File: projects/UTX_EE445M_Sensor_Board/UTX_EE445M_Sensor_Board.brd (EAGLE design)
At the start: 44.5 x 20.9 mm, 26 parts, among them IC1 TM4C123GH6PM, Q1 NX5032GA

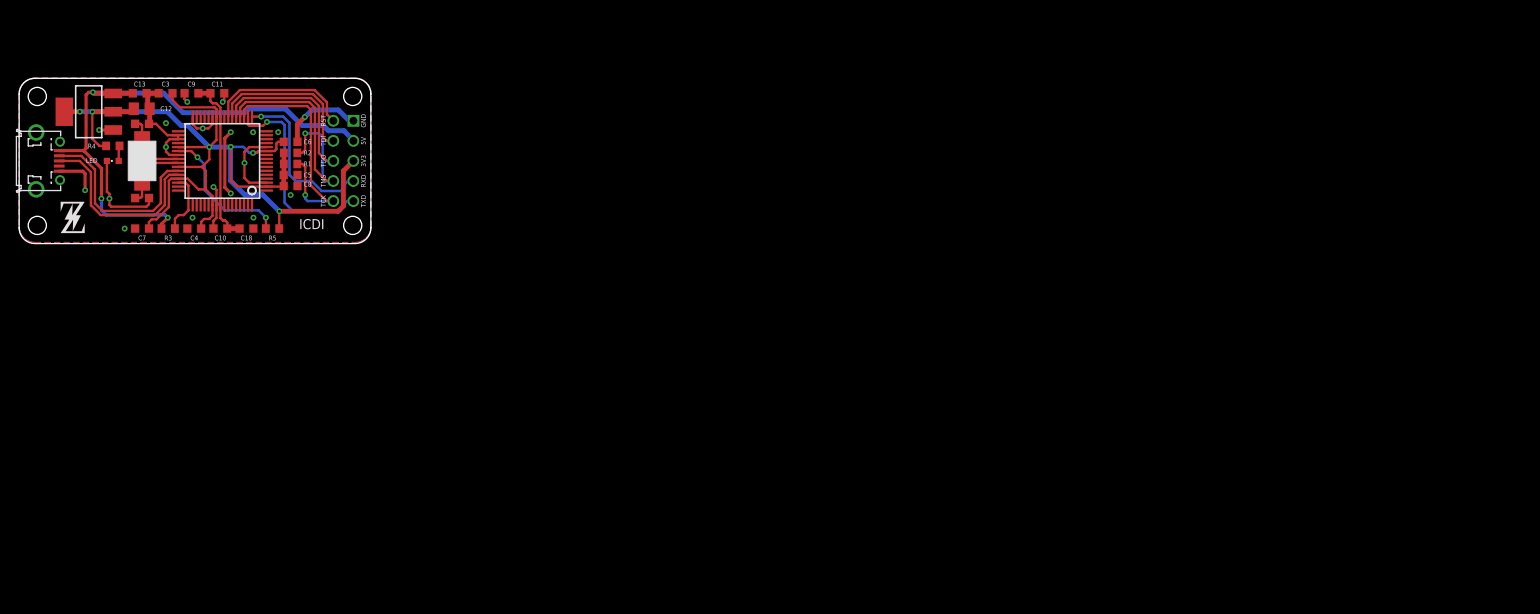
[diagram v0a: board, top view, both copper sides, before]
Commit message: fix some naming and upload UTX EE445M sensor board
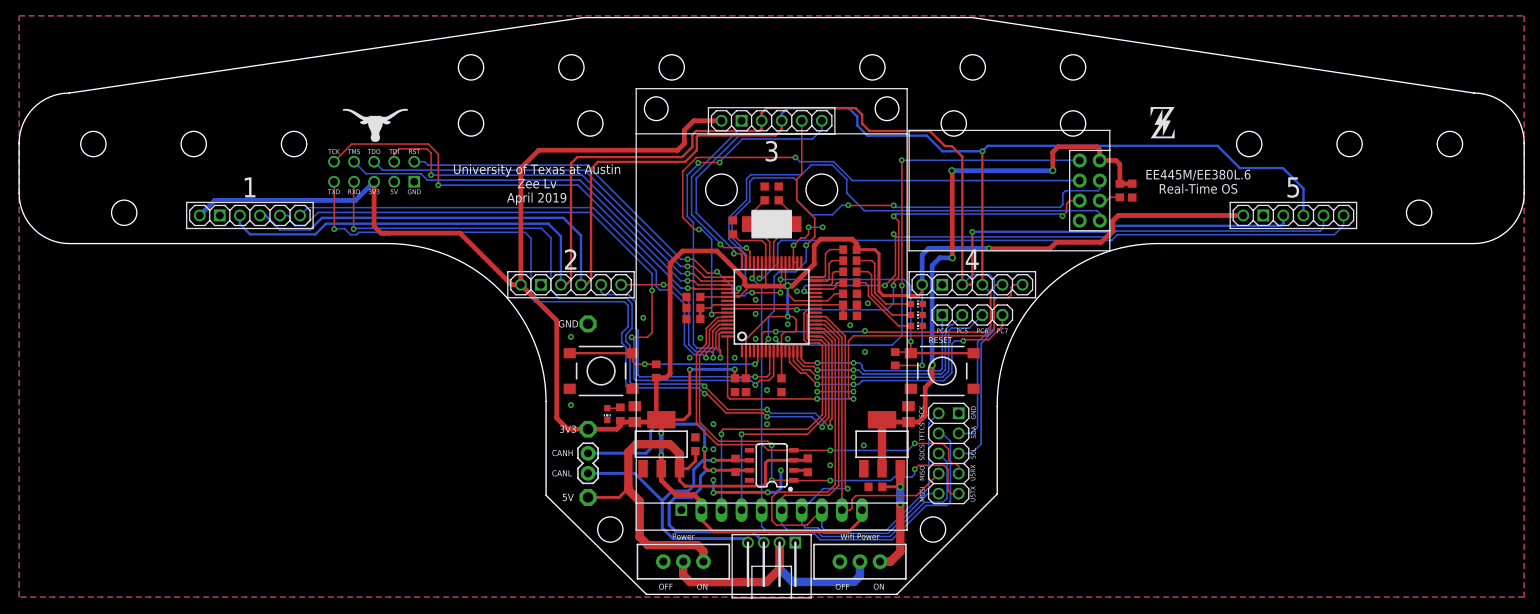
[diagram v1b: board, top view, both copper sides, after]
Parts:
- removed LED: (no value), adafruit:CHIPLED_0603
- added 3V3, 5V, GND: TPPAD1-13, testpad:P1-13
- added BUTTON, RESET: _SWITCH_DTSM-6, Z:_SWITCH_DTSM-6
- added C14: (no value), UT_ECE:C0805K
- added C15: (no value), UT_ECE:C0603K
- added C16, C17: 0.1uF, UT_ECE:C0603K
- added DIS1: ST7735, UT_ECE:ST7735
- added JP1: (no value), UT_ECE:1X02
- added JP2: (no value), UT_ECE:1X04
- added LED1, LED2, LED3, PWR_LED: (no value), led:CHIP-LED0603
- added R6: 120, UT_ECE:R0603
- added R7, R8, R9: 10k, UT_ECE:R0603
- added S1, S2: (no value), SparkFun-Switches:SWITCH_SPDT_PTH_11.6X4.0MM
- added U$10: UTX_EE445M_BOARD_CONNECTOR, Z:_HEADER_2_4X1_ANGLED
- added U$11: LOGIC_ANALYZER_10PIN, Z:LOGIC_ANALYZER_10PIN
- added U$12: (no value), Z:__LOGO_UT_ECE
- added U$13, U$9: _VOLTAGE_REGULATOR_AMS1117, Z:_PACKAGE_SOT223
- added U$14: ESP-01, UT_ECE:ESP8266_01
- added U$5, U$6: LIDAR_VL53L0X_ATK_VERT, Z:LIDAR_VL53L0X_ATK_VERT
- added U$7: (no value), Z:LOGO_LORNHORNS
- added U$8: (no value), Z:LOGO_Z_3X4
- added U4: MCP2551PSOIC, UT_ECE:SO08
- R1, R2, R4: value 10k -> 470
- R3: value 330 -> 470; device UT_ECE:R0603 -> rcl:R0603
- R5: value 10k -> 1M
- U$1: value USB_MICRO_PTH -> JTAG_SERIAL; device Z:USB_MICRO_PTH -> Z:JTAG_SERIAL_PTH
- U$2: value JTAG_SERIAL -> LIDAR_VL53L0X_ATK_VERT; device Z:JTAG_SERIAL_PTH -> Z:LIDAR_VL53L0X_ATK_VERT
- U$3: value (none) -> LIDAR_VL53L0X_ATK_VERT; device Z:__LOGO_Z -> Z:LIDAR_VL53L0X_ATK_VERT
- U$4: value _VOLTAGE_REGULATOR_AMS1117 -> LIDAR_VL53L0X_ATK_VERT; device Z:_PACKAGE_SOT223 -> Z:LIDAR_VL53L0X_ATK_VERT
- moved R4 94.4 mm to (105.2, -2.16)
- moved C3 90.3 mm to (105.2, -6.35), turned to 0 degrees
- moved C9 87.5 mm to (105.2, -7.75), turned to 0 degrees
- moved U$4 86.4 mm to (95.2, 15.5), turned to 0 degrees
- moved C11 84.9 mm to (105.2, -9.14)
- moved C13 83.2 mm to (85.6, -25.4), turned to 90 degrees
- moved C1 81.1 mm to (96.1, 6.35), turned to 90 degrees
- moved Q1 80.1 mm to (95.2, 2.46), turned to 180 degrees
- moved C2 78.8 mm to (94.4, 6.35), turned to 90 degrees
- moved C7 74.8 mm to (90.3, 2.06), turned to 90 degrees
- moved C12 73.4 mm to (77.9, -21.6), turned to 90 degrees
- moved R5 73.1 mm to (105.2, -0.76), turned to 180 degrees
- moved R1 72.4 mm to (105.2, -4.95)
- moved R2 72.4 mm to (105.2, -3.56)
- moved IC1 71.9 mm to (95.2, -8.00), turned to 0 degrees
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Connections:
- net LDO renamed VDDC
- removed net UART0_RX: IC1.17, U$2.RXD
- removed net UART0_TX: IC1.18, U$2.TXD
- removed net USB_DM: IC1.43, U$1.2
- removed net USB_DP: IC1.44, U$1.3
- new net CANH: JP1.2, R6.2, U$10.2, U4.7
- new net CANL: JP1.1, R6.1, U$10.1, U4.6
- new net ESP_3V3: C14.1, C16.1, R9.2, U$13.2, U$13.4, U$14.VCC
- new net ESP_5V: C15.1, S2.1, U$13.3
- new net ESP_GPIO0: IC1.58, U$14.GPIO_0
- new net ESP_GPIO2: IC1.57, U$14.GPIO_2
- new net ESP_RESET: IC1.46, U$14.RESET
- new net I2C0_SCL: IC1.47, U$11.8, U$2.SCL, U$3.SCL, U$4.SCL, U$5.SCL, U$6.SCL
- new net I2C0_SDA: IC1.48, U$11.9, U$2.SDA, U$3.SDA, U$4.SDA, U$5.SDA, U$6.SDA
- new net LOGIC1: IC1.16, JP2.1
- new net LOGIC2: IC1.15, JP2.2
- new net LOGIC3: IC1.14, JP2.3
- new net LOGIC4: IC1.13, JP2.4
- new net N$18: U$1.5V
- new net N$19: IC1.32, R5.2
- new net N$3: S1.3
- new net N$6: PWR_LED.A, R3.1
- new net N$7: LED2.A, R2.1
- new net N$8: LED3.A, R4.1
- new net PF1: IC1.29, R1.2
- new net PF2: IC1.30, R2.2
- new net PF3: IC1.31, R4.2
- new net PF4: BUTTON.1, BUTTON.2, IC1.5, R8.2
- new net RXD: IC1.18, U$1.RXD
- new net SD_CS: DIS1.5, IC1.45, U$11.2
- new net SSI0_MISO: DIS1.9, IC1.21, U$11.4
- new net SSI0_MOSI: DIS1.7, IC1.22, U$11.5
- new net SSI0_SCK: DIS1.8, IC1.19, U$11.1
- new net TFT_CS: DIS1.6, IC1.20, U$11.3
- new net TFT_D/C: DIS1.4, IC1.23
- new net TFT_RESET: DIS1.3, IC1.24
- new net TXD: IC1.17, U$1.TXD
- new net UART2_RX: IC1.53, U$14.TX
- new net UART2_TX: IC1.10, U$14.RX
- new net UART5_RX: IC1.59, U$11.7, U4.4
- new net UART5_TX: IC1.60, U$11.6, U4.1
- new net VIN: S1.2, S2.2, U$10.3
- new net VX_INT1: IC1.9, U$2.INT
- new net VX_INT2: IC1.8, U$3.INT
- new net VX_INT3: IC1.7, U$4.INT
- new net VX_INT4: IC1.6, U$5.INT
- new net VX_INT5: IC1.28, U$6.INT
- new net XSHUT1: IC1.61, U$2.XSH
- new net XSHUT2: IC1.62, U$3.XSH
- new net XSHUT3: IC1.63, U$4.XSH
- new net XSHUT4: IC1.64, U$5.XSH
- new net XSHUT5: IC1.43, U$6.XSH
- net 3V3: now also 3V3.TP, DIS1.10, DIS1.2, R3.2, R5.1, R7.1, R8.1, U$1.3V3, U$2.VCC, U$3.VCC, U$4.VCC, U$5.VCC, U$6.VCC, U$9.2, U$9.4; no longer IC1.45, R1.2, R2.2, R4.2, R5.2, U$2.3V3, U$4.2, U$4.4
- net 5V: now also 5V.TP, C17.1, S1.1, U$9.3, U4.3; no longer R3.2, U$1.1, U$2.5V, U$4.3
- net GND: now also BUTTON.3, BUTTON.4, C14.2, C15.2, C16.2, C17.2, DIS1.1, GND.TP, LED1.C, LED2.C, LED3.C, PWR_LED.C, RESET.3, RESET.4, U$1.GND, U$10.4, U$11.10, U$13.1, U$14.GND, U$3.GND, U$4.GND, U$5.GND, U$6.GND, U$9.1, U4.2, U4.8; no longer IC1.32, LED.C, U$1.5, U$4.1
- net N$1: now also R9.1, U$14.CH_PD; no longer LED.A, R4.1
- net N$2: now also S2.3; no longer IC1.46, R3.1
- net N$4: now also LED1.A, R1.1; no longer IC1.38, R5.1
- net RST: now also IC1.38, R7.2, RESET.1, RESET.2, U$1.RST; no longer IC1.23, U$2.RST
- net TCK: now also IC1.52, U$1.TCK; no longer IC1.19, R1.1, U$2.TCK
- net TDI: now also IC1.50, U$1.TDI; no longer IC1.22, U$2.TDI
- net TDO: now also IC1.49, U$1.TDO; no longer IC1.21, U$2.TDO
- net TMS: now also IC1.51, U$1.TMS; no longer IC1.20, R2.1, U$2.TMS
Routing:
- net I2C0_SCL: track 0.00 -> 245.3 mm, vias 0 -> 2
- net 3V3: track 130.3 -> 367.1 mm, vias 6 -> 8
- net I2C0_SDA: track 0.00 -> 235.8 mm, vias 0 -> 2
- net TXD: track 0.00 -> 102.6 mm, vias 0 -> 4
- net RXD: track 0.00 -> 100.8 mm, vias 0 -> 4
- net VX_INT1: track 0.00 -> 89.1 mm, vias 0 -> 3
- net XSHUT5: track 0.00 -> 81.6 mm, vias 0 -> 1
- net VX_INT5: track 0.00 -> 76.1 mm, vias 0 -> 3
- net ESP_3V3: track 0.00 -> 75.1 mm, vias 0 -> 4
- net RST: track 18.3 -> 93.4 mm, vias 0 -> 6
- net ESP_GPIO0: track 0.00 -> 74.4 mm, vias 0 -> 3
- net SD_CS: track 0.00 -> 70.1 mm, vias 0 -> 1
- net XSHUT1: track 0.00 -> 69.8 mm, vias 0 -> 1
- net SSI0_SCK: track 0.00 -> 68.3 mm
- net UART2_RX: track 0.00 -> 67.8 mm, vias 0 -> 1
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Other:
- board size 44.5 x 20.9 mm -> 190.5 x 73 mm
- board text added: "1"
- board text added: "2"
- board text added: "3"
- board text added: "4"
- board text added: "5"
- board text added: "CANH"
- board text added: "CANL"
- board text added: "EE445M/EE380L.6 Real-Time OS"
- board text added: "GND"
- board text added: "MISO"
- board text added: "MOSI"
- board text added: "OFF ON"
- board text added: "PC4"
- board text added: "PC5"
- board text added: "PC6"
- board text added: "PC7"
- board text added: "Power"
- board text added: "SCK"
- board text added: "SCL"
- board text added: "SDA"
- board text added: "SDCS"
- board text added: "TFTCS"
- board text added: "U5RX"
- board text added: "U5TX"
- board text added: "University of Texas at Austin Zee Lv April 2019"
- board text added: "Wifi Power"
- board text removed: "ICDI"
- board text removed: "Mar 2019 Zee Lv"

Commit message: add EE445M motor board
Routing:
- net N$4: track 9.89 -> 11.7 mm
- net N$7: track 10.6 -> 11.8 mm
- net 3V3: track 367.1 -> 366.5 mm
- net GND: track 27.0 -> 26.9 mm, vias 30 -> 33
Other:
- board text added: "University of Texas at Austin Mohammad Behnia Zee Lv Tariq Muhanna Genki Oji Abhishek Ramani April 2019"
- board text removed: "University of Texas at Austin Zee Lv April 2019"
